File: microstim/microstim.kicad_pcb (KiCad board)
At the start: 2 copper layers, 189.9 x 76.2 mm, 93 parts, among them J1 Conn_Coaxial, J10 Conn_Coaxial, J11 Screw_Terminal_01x02, J12 Conn_Coaxial, J2 Conn_Coaxial, J3 Screw_Terminal_01x02, J4 Screw_Terminal_01x02, J5 Conn_Coaxial, J6 Conn_Coaxial, J7 Screw_Terminal_01x02, J8 Screw_Terminal_01x02, J9 Screw_Terminal_01x02, SW1 SW_Push, SW2 SW_Push, U1 Teensy3.5, U10 AD7321, U11 LTC2057, U12 LTC2057, U13 DG509ACWE, U14 DG509ACWE, U15 LT1167, U16 LT1167, U17 LM358, U18 DG509ACWE, U19 DG509ACWE, U2 CC3-0512DF-E, U3 L78L05_SO8, U4 L78L12_SO8, U5 ISO7760, U6 ISO7760, U7 ISO7341C, U8 L79L12_SO8, U9 MCP4922

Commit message: added board name in silkscreen
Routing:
- net ISENSE0: track 160.5 -> 134.1 mm
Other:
- board text added: "microStim v0.1 original design by jon newman modified by nate cermak"
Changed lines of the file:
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@@
   (general
     (thickness 1.6)
-    (drawings 4)
-    (tracks 908)
+    (drawings 5)
+    (tracks 900)
     (zones 0)
     (modules 93)
@@
     )
   )
+  (gr_text "microStim v0.1\noriginal design by jon newman\nmodified by nate cermak" (at 204.724 91.821) (layer F.SilkS)
+    (effects (font (size 1.5 1.5) (thickness 0.3)))
+  )
   (gr_line (start 65.913 21.59) (end 65.913 97.79) (layer Edge.Cuts) (width 0.15))
   (gr_line (start 255.778 21.59) (end 65.913 21.59) (layer Edge.Cuts) (width 0.15))
@@
   (segment (start 156.748 82.52) (end 154.813 84.455) (width 0.25) (layer F.Cu) (net 81))
   (segment (start 236.916 55.118) (end 236.916 53.848) (width 0.25) (layer F.Cu) (net 82))
-  (segment (start 236.916 53.298) (end 238.652 51.562) (width 0.25) (layer F.Cu) (net 82))
-  (segment (start 236.916 53.848) (end 236.916 53.298) (width 0.25) (layer F.Cu) (net 82))
-  (segment (start 245.109494 51.562) (end 245.363494 51.308) (width 0.25) (layer F.Cu) (net 82))
-  (segment (start 238.652 51.562) (end 245.109494 51.562) (width 0.25) (layer F.Cu) (net 82))
-  (segment (start 238.178408 53.930408) (end 241.280999 57.032999) (width 0.25) (layer F.Cu) (net 82))
   (segment (start 239.0816 52.12799) (end 247.3284 52.12799) (width 0.25) (layer F.Cu) (net 82))
-  (segment (start 241.280999 57.032999) (end 241.299589 57.032999) (width 0.25) (layer F.Cu) (net 82))
-  (segment (start 238.178408 51.562) (end 238.178408 53.930408) (width 0.25) (layer F.Cu) (net 82))
-  (segment (start 245.109494 51.562) (end 238.178408 51.562) (width 0.25) (layer F.Cu) (net 82))
-  (segment (start 241.299589 57.032999) (end 238.81799 54.5514) (width 0.25) (layer F.Cu) (net 82))
   (segment (start 247.59201 82.2284) (end 242.95241 86.868) (width 0.25) (layer F.Cu) (net 82))
-  (segment (start 238.81799 54.5514) (end 238.81799 52.3916) (width 0.25) (layer F.Cu) (net 82))
   (segment (start 247.3284 52.12799) (end 247.59201 52.3916) (width 0.25) (layer F.Cu) (net 82))
-  (segment (start 238.81799 52.3916) (end 239.0816 52.12799) (width 0.25) (layer F.Cu) (net 82))
   (segment (start 247.59201 52.3916) (end 247.59201 82.2284) (width 0.25) (layer F.Cu) (net 82))
   (segment (start 242.95241 86.868) (end 171.958 86.868) (width 0.25) (layer F.Cu) (net 82))
@@
   (segment (start 160.88 87.22) (end 160.88 86.245) (width 0.25) (layer F.Cu) (net 82))
   (segment (start 162.052 88.392) (end 160.88 87.22) (width 0.25) (layer F.Cu) (net 82))
+  (segment (start 238.08601 52.12799) (end 239.0816 52.12799) (width 0.25) (layer F.Cu) (net 82))
+  (segment (start 236.916 53.298) (end 238.08601 52.12799) (width 0.25) (layer F.Cu) (net 82))
+  (segment (start 236.916 53.848) (end 236.916 53.298) (width 0.25) (layer F.Cu) (net 82))
   (segment (start 242.316 56.388) (end 242.316 55.118) (width 0.25) (layer F.Cu) (net 83))
   (segment (start 167.755 85.77) (end 166.78 85.77) (width 0.25) (layer F.Cu) (net 83))

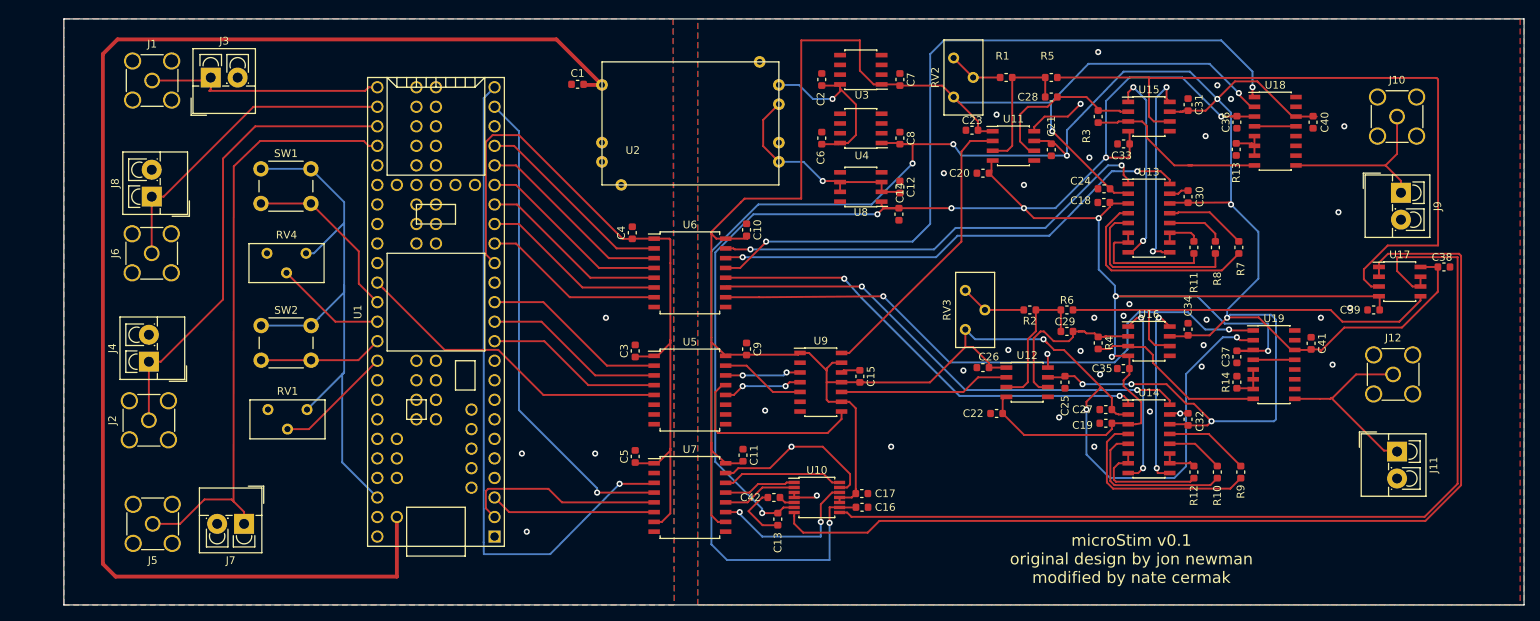
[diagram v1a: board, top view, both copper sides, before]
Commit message: added mounting holes
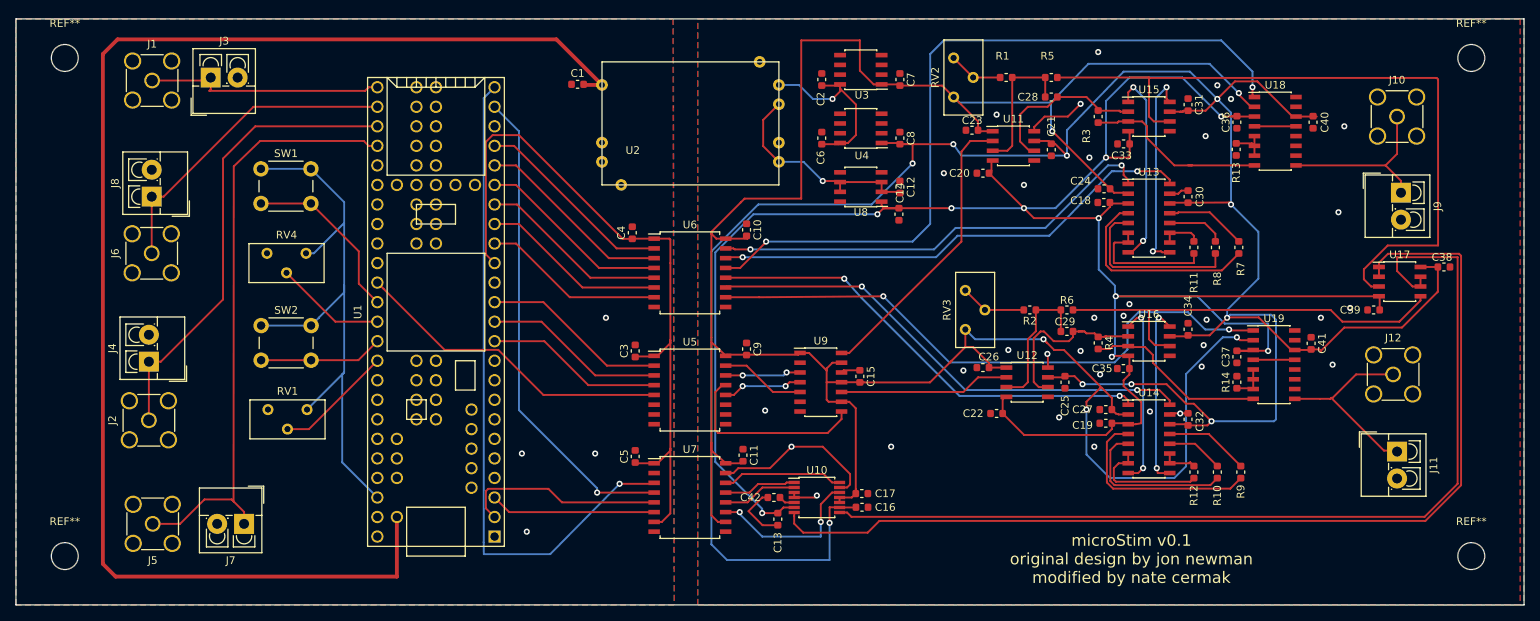
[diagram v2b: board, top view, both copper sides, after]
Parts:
- added REF**: MountingHole_3.5mm, MountingHole:MountingHole_3.5mm, F.Cu at (248.9, 91.4)
- added REF**: MountingHole_3.5mm, MountingHole:MountingHole_3.5mm, F.Cu at (248.9, 26.7)
- added REF**: MountingHole_3.5mm, MountingHole:MountingHole_3.5mm, F.Cu at (66.0, 26.7)
- added REF**: MountingHole_3.5mm, MountingHole:MountingHole_3.5mm, F.Cu at (66.0, 91.4)
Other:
- board size 189.9 x 76.2 mm -> 196.1 x 76.2 mm
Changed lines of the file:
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@@
     (tracks 900)
     (zones 0)
-    (modules 93)
+    (modules 97)
     (nets 156)
   )
@@
     )
   )
+  (module MountingHole:MountingHole_3.5mm (layer F.Cu)
+    (at 248.92 91.44)
+    (descr "Mounting Hole 3.5mm, no annular")
+    (tags "mounting hole 3.5mm no annular")
+    (attr virtual)
+    (fp_text reference REF** (at 0 -4.5) (layer F.SilkS)
+      (effects (font (size 1 1) (thickness 0.15)))
+    )
+    (fp_text value MountingHole_3.5mm (at 0 4.5) (layer F.Fab)
+      (effects (font (size 1 1) (thickness 0.15)))
+    )
+    (fp_circle (center 0 0) (end 3.75 0) (layer F.CrtYd) (width 0.05))
+    (fp_circle (center 0 0) (end 3.5 0) (layer Cmts.User) (width 0.15))
+    (fp_text user %R (at 0.3 0) (layer F.Fab)
+      (effects (font (size 1 1) (thickness 0.15)))
+    )
+    (pad 1 np_thru_hole circle (at 0 0) (size 3.5 3.5) (drill 3.5) (layers *.Cu *.Mask))
+  )
+  (module MountingHole:MountingHole_3.5mm (layer F.Cu)
+    (at 248.92 26.67)
+    (descr "Mounting Hole 3.5mm, no annular")
+    (tags "mounting hole 3.5mm no annular")
+    (attr virtual)
+    (fp_text reference REF** (at 0 -4.5) (layer F.SilkS)
+      (effects (font (size 1 1) (thickness 0.15)))
+    )
+    (fp_text value MountingHole_3.5mm (at 0 4.5) (layer F.Fab)
+      (effects (font (size 1 1) (thickness 0.15)))
+    )
+    (fp_circle (center 0 0) (end 3.75 0) (layer F.CrtYd) (width 0.05))
+    (fp_circle (center 0 0) (end 3.5 0) (layer Cmts.User) (width 0.15))
+    (fp_text user %R (at 0.3 0) (layer F.Fab)
+      (effects (font (size 1 1) (thickness 0.15)))
+    )
+    (pad 1 np_thru_hole circle (at 0 0) (size 3.5 3.5) (drill 3.5) (layers *.Cu *.Mask))
+  )
+  (module MountingHole:MountingHole_3.5mm (layer F.Cu)
+    (at 66.04 26.67)
+    (descr "Mounting Hole 3.5mm, no annular")
+    (tags "mounting hole 3.5mm no annular")
+    (attr virtual)
+    (fp_text reference REF** (at 0 -4.5) (layer F.SilkS)
+      (effects (font (size 1 1) (thickness 0.15)))
+    )
+    (fp_text value MountingHole_3.5mm (at 0 4.5) (layer F.Fab)
+      (effects (font (size 1 1) (thickness 0.15)))
+    )
+    (fp_circle (center 0 0) (end 3.75 0) (layer F.CrtYd) (width 0.05))
+    (fp_circle (center 0 0) (end 3.5 0) (layer Cmts.User) (width 0.15))
+    (fp_text user %R (at 0.3 0) (layer F.Fab)
+      (effects (font (size 1 1) (thickness 0.15)))
+    )
+    (pad 1 np_thru_hole circle (at 0 0) (size 3.5 3.5) (drill 3.5) (layers *.Cu *.Mask))
+  )
+  (module MountingHole:MountingHole_3.5mm (layer F.Cu)
+    (at 66.04 91.44)
+    (descr "Mounting Hole 3.5mm, no annular")
+    (tags "mounting hole 3.5mm no annular")
+    (attr virtual)
+    (fp_text reference REF** (at 0 -4.5) (layer F.SilkS)
+      (effects (font (size 1 1) (thickness 0.15)))
+    )
+    (fp_text value MountingHole_3.5mm (at 0 4.5) (layer F.Fab)
+      (effects (font (size 1 1) (thickness 0.15)))
+    )
+    (fp_circle (center 0 0) (end 3.75 0) (layer F.CrtYd) (width 0.05))
+    (fp_circle (center 0 0) (end 3.5 0) (layer Cmts.User) (width 0.15))
+    (fp_text user %R (at 0.3 0) (layer F.Fab)
+      (effects (font (size 1 1) (thickness 0.15)))
+    )
+    (pad 1 np_thru_hole circle (at 0 0) (size 3.5 3.5) (drill 3.5) (layers *.Cu *.Mask))
+  )
   (gr_text "microStim v0.1\noriginal design by jon newman\nmodified by nate cermak" (at 204.724 91.821) (layer F.SilkS)
     (effects (font (size 1.5 1.5) (thickness 0.3)))
   )
-  (gr_line (start 65.913 21.59) (end 65.913 97.79) (layer Edge.Cuts) (width 0.15))
-  (gr_line (start 255.778 21.59) (end 65.913 21.59) (layer Edge.Cuts) (width 0.15))
+  (gr_line (start 59.69 21.59) (end 59.69 97.79) (layer Edge.Cuts) (width 0.15))
+  (gr_line (start 255.778 21.59) (end 59.69 21.59) (layer Edge.Cuts) (width 0.15))
   (gr_line (start 255.778 97.79) (end 255.778 21.59) (layer Edge.Cuts) (width 0.15))
-  (gr_line (start 65.913 97.79) (end 255.778 97.79) (layer Edge.Cuts) (width 0.15))
+  (gr_line (start 59.69 97.79) (end 255.778 97.79) (layer Edge.Cuts) (width 0.15))
   (segment (start 203.86 44.323) (end 203.733 44.196) (width 0.25) (layer F.Cu) (net 1))
   (segment (start 204.31 44.323) (end 203.86 44.323) (width 0.25) (layer F.Cu) (net 1))
@@
   (segment (start 101.219 60.96) (end 94.869 54.61) (width 0.25) (layer F.Cu) (net 149))
   (segment (start 106.68 60.96) (end 101.219 60.96) (width 0.25) (layer F.Cu) (net 149))
-  (zone (net 16) (net_name GND) (layer F.Cu) (hatch edge 0.508)
+  (zone (net 2) (net_name GNDREF) (layer F.Cu) (hatch edge 0.508)
     (connect_pads (clearance 0.508))
     (min_thickness 0.254)
@@
     (polygon
       (pts
-        (xy 65.913 21.59) (xy 145.116061 21.59) (xy 145.288 97.79) (xy 65.913 97.79) (xy 65.913 42.164)
+        (xy 148.336 21.59) (xy 255.27 21.59) (xy 255.27 97.79) (xy 148.336 97.79)
       )
     )
   )
-  (zone (net 2) (net_name GNDREF) (layer F.Cu) (hatch edge 0.508)
+  (zone (net 2) (net_name GNDREF) (layer B.Cu) (hatch edge 0.508)
     (connect_pads (clearance 0.508))
     (min_thickness 0.254)
@@
     (polygon
       (pts
-        (xy 148.336 21.59) (xy 255.27 21.59) (xy 255.27 97.79) (xy 148.336 97.79)
+        (xy 148.336 21.59) (xy 255.778 21.59) (xy 255.778 97.79) (xy 148.336 97.79)
       )
     )
   )
-  (zone (net 2) (net_name GNDREF) (layer B.Cu) (hatch edge 0.508)
+  (zone (net 16) (net_name GND) (layer B.Cu) (hatch edge 0.508)
     (connect_pads (clearance 0.508))
     (min_thickness 0.254)
@@
     (polygon
       (pts
-        (xy 148.336 21.59) (xy 255.778 21.59) (xy 255.778 97.79) (xy 148.336 97.79)
+        (xy 59.69 21.59) (xy 145.161 21.59) (xy 145.288 97.79) (xy 59.69 97.79)
       )
     )
   )
-  (zone (net 16) (net_name GND) (layer B.Cu) (hatch edge 0.508)
+  (zone (net 16) (net_name GND) (layer F.Cu) (hatch edge 0.508)
     (connect_pads (clearance 0.508))
     (min_thickness 0.254)
@@
     (polygon
       (pts
-        (xy 65.913 21.59) (xy 145.161 21.59) (xy 145.288 97.79) (xy 65.913 97.79)
+        (xy 59.69 21.59) (xy 145.116061 21.59) (xy 145.288 97.79) (xy 59.69 97.79) (xy 59.69 42.164)
       )
     )

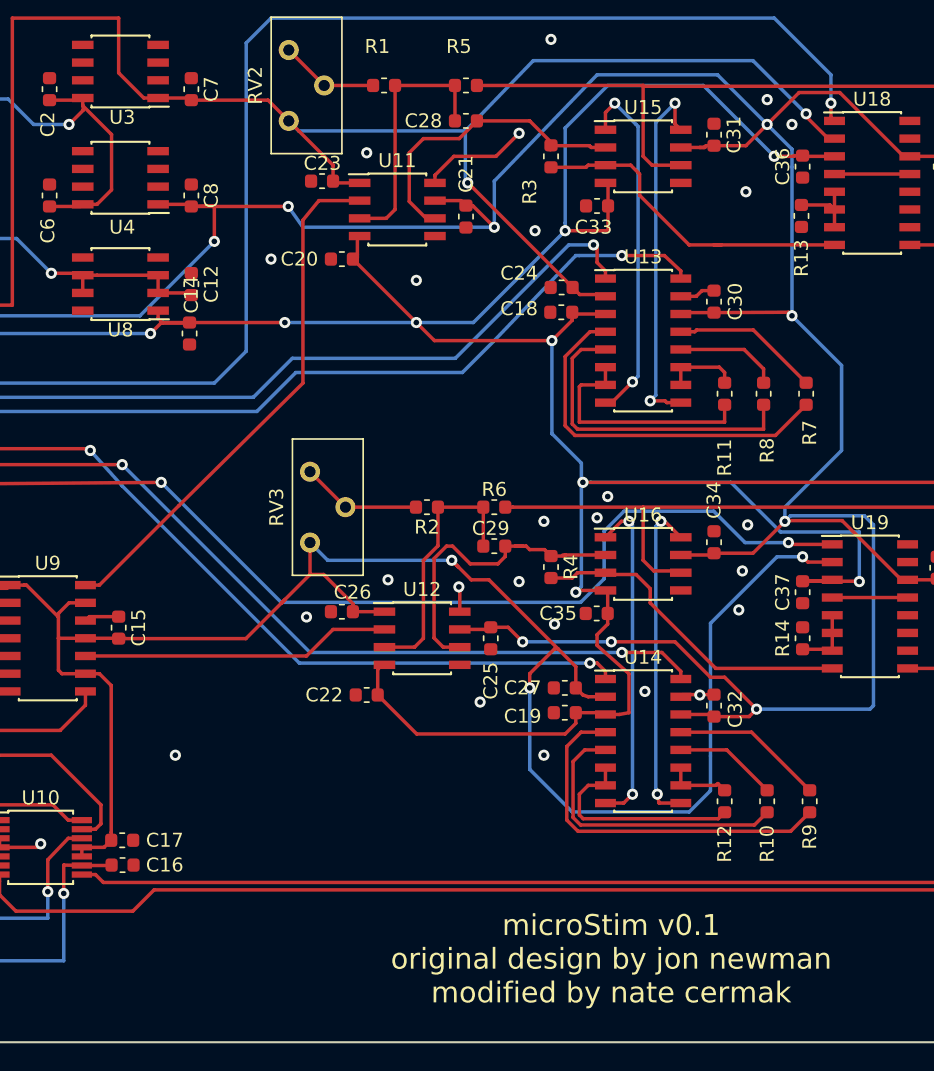
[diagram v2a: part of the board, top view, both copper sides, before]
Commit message: fixed some op-amps inserted backwards. also had to recommit everything due to OS upgrade and HD backup.
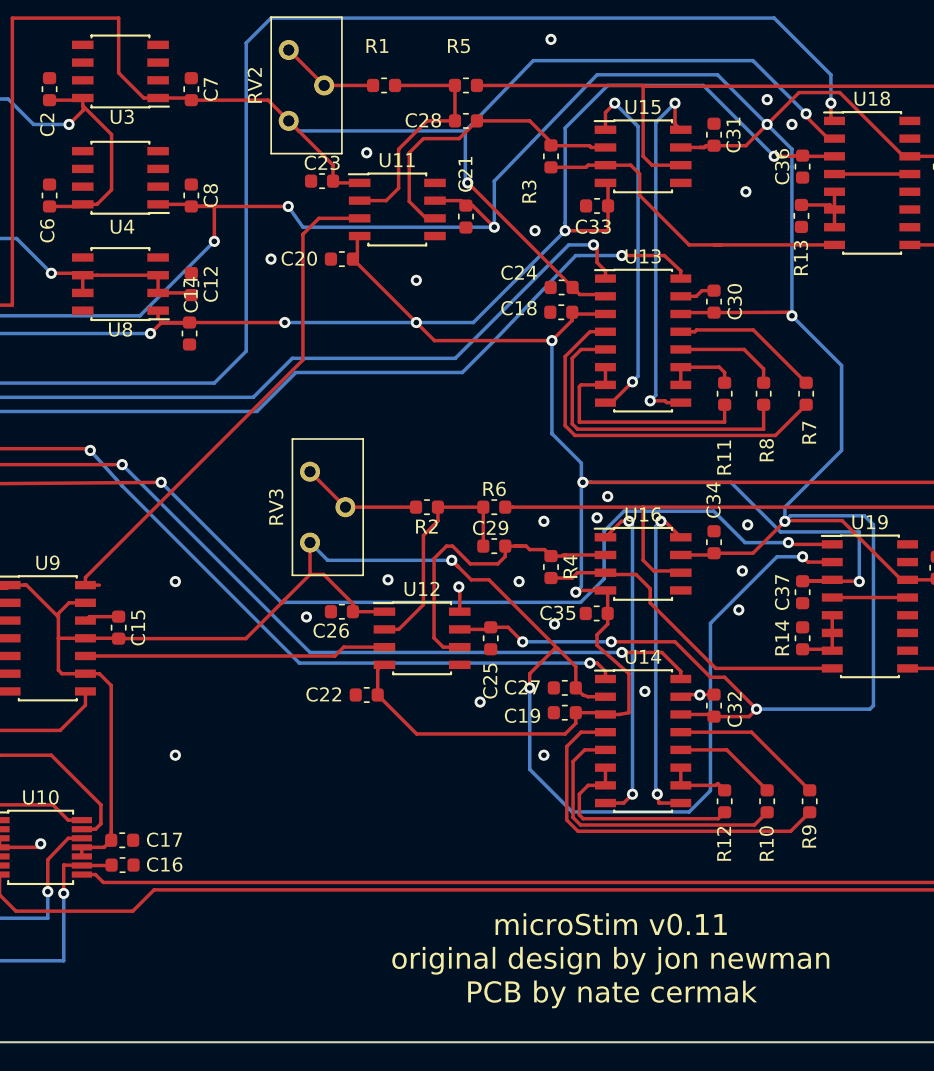
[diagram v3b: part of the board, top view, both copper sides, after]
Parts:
- turned C26 to 180 degrees
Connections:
- C26 pad 1: GNDREF -> +5V
- C26 pad 2: +5V -> GNDREF
- U11 pad 2: Net-(U11-Pad2) -> Net-(C28-Pad2)
- U11 pad 3: Net-(C28-Pad2) -> Net-(U11-Pad3)
- U12 pad 2: Net-(U12-Pad2) -> Net-(C29-Pad2)
- U12 pad 3: Net-(C29-Pad2) -> Net-(U12-Pad3)
- U15 pad 2: Net-(C28-Pad1) -> Net-(R3-Pad2)
- U15 pad 3: Net-(R3-Pad2) -> Net-(C28-Pad1)
- U16 pad 2: Net-(C29-Pad1) -> Net-(R4-Pad2)
- U16 pad 3: Net-(R4-Pad2) -> Net-(C29-Pad1)
- U9 pad 10: Net-(U12-Pad2) -> Net-(U12-Pad3)
- U9 pad 14: Net-(U11-Pad2) -> Net-(U11-Pad3)
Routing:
- net Net-(U11-Pad2): track 37.8 -> 0.00 mm
- net Net-(U11-Pad3): track 0.00 -> 37.1 mm
- net Net-(U12-Pad2): track 22.1 -> 0.00 mm
- net Net-(U12-Pad3): track 0.00 -> 21.7 mm
- net GNDREF: track 50.6 -> 42.8 mm
- net Net-(C29-Pad2): track 19.1 -> 17.0 mm
- net Net-(C28-Pad2): track 18.7 -> 17.7 mm
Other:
- board text added: "microStim v0.11 original design by jon newman PCB by nate cermak"
- board text removed: "microStim v0.1 original design by jon newman modified by nate cermak"
